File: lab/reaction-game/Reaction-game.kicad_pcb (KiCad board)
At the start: 2 copper layers, 92 x 72 mm, 10 parts, among them U1 atmega328p

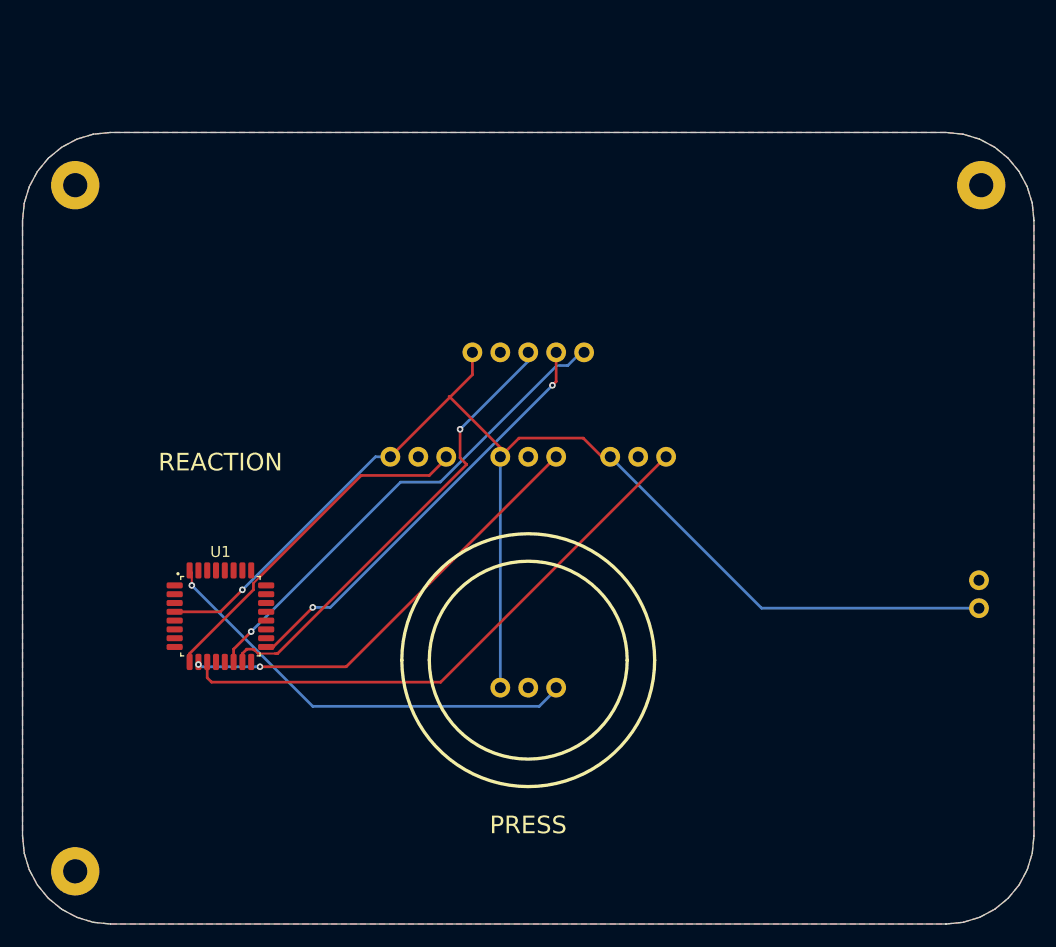
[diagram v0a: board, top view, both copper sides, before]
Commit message: lab: every board is a real board: an Arduino Nano and registry parts, routed, ready to order
The lab boards ran on simulation-only envelopes (labMcu, labDisplay, a battery). Now each is
an Arduino Nano on two sockets on the back (flashed over its USB, the image the app builds),
its lights LEDs through 1 kΩ, its knobs PTV09A pots, its display the MAX7219 eight-digit
module, its sensors an SHT31 and an SCD40 with their datasheets' support circuits, the FTDI
header for the serial console; the servo boards take 5 V on a screw terminal with a bulk
capacitor. All ten check complete with no errors or warnings, their firmware unchanged
(serial-device now on the 328P), and run in the lab without a fault (3 s each, dev host).

The registry: every interactive board must be ready to order and flash (publish.mjs refuses
one that is not; status simulation-only removed).

Claude-Session: https://claude.ai/code/session_01ATmMmxyrWxFwR3nTdXUrcx
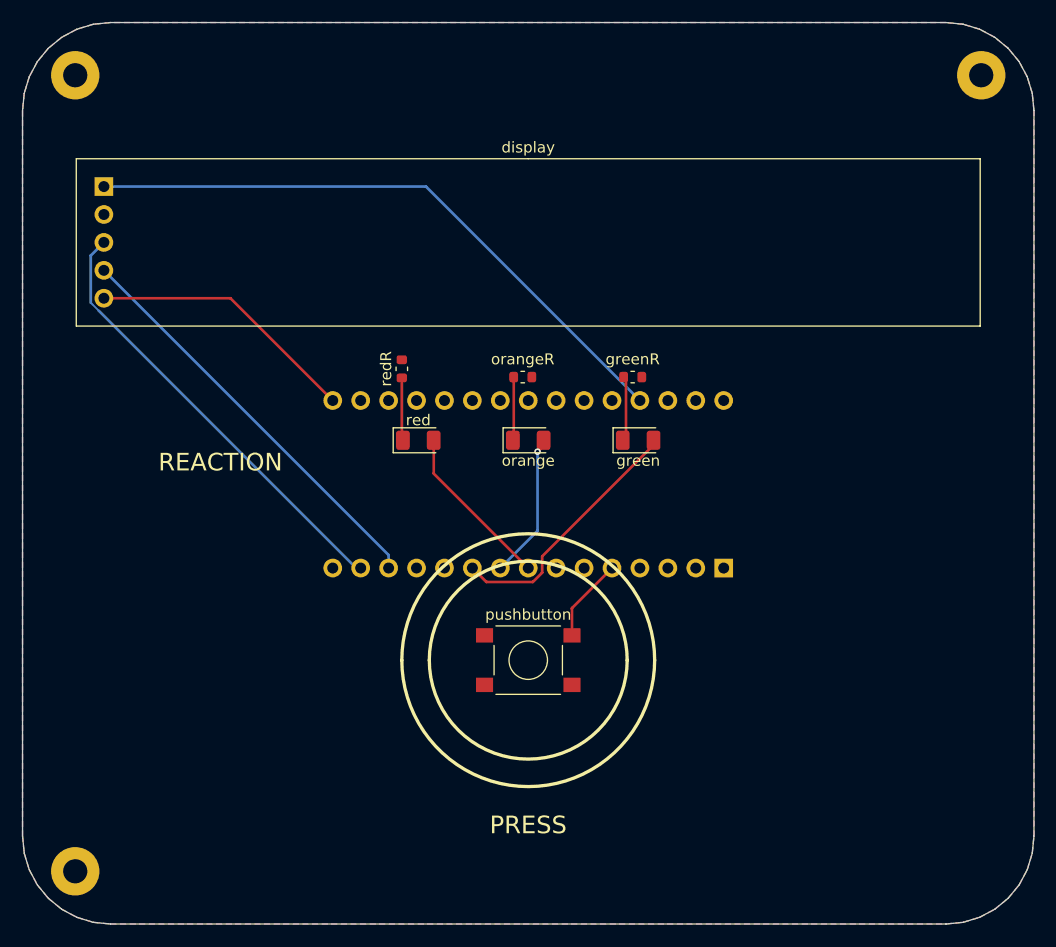
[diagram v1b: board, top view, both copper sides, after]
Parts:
- removed battery: battery, Regulated battery module
- removed button: button, Button module
- removed the display at (146.0, 142.0)
- removed the green at (156.0, 156.0)
- removed the orange at (146.0, 156.0)
- removed the red at (136.0, 156.0)
- added display: MAX7219 8-digit 7-segment LED display module, MAX7219_8digit_Module_Socket_1x05_P2.54mm, F.Cu at (146.0, 138.0)
- added green: green, LED_1206_3216Metric, F.Cu at (156.0, 156.0)
- added greenR: 1kohm, R_0603_1608Metric, F.Cu at (155.5, 150.2)
- added orange: orange, LED_1206_3216Metric, F.Cu at (146.0, 156.0)
- added orangeR: 1kohm, R_0603_1608Metric, F.Cu at (145.5, 150.2)
- added pushbutton: PTS645SM43SMTR92 LFS, SW_Tactile_SPST_6x6mm_SMD, F.Cu at (146.0, 176.0)
- added red: red, LED_1206_3216Metric, F.Cu at (136.0, 156.0)
- added redR: 1kohm, R_0603_1608Metric, F.Cu at (134.5, 149.5)
- U1: value atmega328p -> A000005; footprint TQFP-32_7x7mm_P0.8mm -> Arduino_Nano_Socket_2x15_P2.54mm_W15.24mm; moved to B.Cu
- moved U1 30.5 mm to (146.0, 160.0), turned to 90 degrees
- moved H2 10.0 mm to (104.8, 122.8)
- moved H3 10.0 mm to (187.2, 122.8)
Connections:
- U1 pad 10: ORANGE -> GREEN
- U1 pad 11: GREEN -> (no net)
- U1 pad 13: (no net) -> LOAD
- U1 pad 14: LOAD -> MOSI
- U1 pad 15: MOSI -> (no net)
- U1 pad 16: (no net) -> SCK
- U1 pad 17: SCK -> (no net)
- U1 pad 27: (no net) -> V5
- U1 pad 29: (no net) -> GND
- U1 pad 3: GND -> (no net)
- U1 pad 4: V5 -> GND
- U1 pad 5: (no net) -> PRESS
- U1 pad 8: (no net) -> RED
- U1 pad 9: RED -> ORANGE
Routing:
- net V5: track 117.1 -> 56.8 mm, vias 1 -> 0
- net PRESS: track 39.9 -> 7.64 mm, vias 1 -> 0
- net GREEN: track 51.8 -> 23.5 mm
- net ORANGE: track 40.5 -> 13.3 mm, vias 2 -> 1
- net RED: track 32.0 -> 15.2 mm
- net SCK: track 39.0 -> 24.7 mm, vias 2 -> 0
- net LOAD: track 44.2 -> 37.8 mm, vias 1 -> 0
- net GREEN_K: track 0.00 -> 5.96 mm
- net ORANGE_K: track 0.00 -> 5.78 mm
- net RED_K: track 0.00 -> 5.72 mm
- net MOSI: track 41.6 -> 40.5 mm, vias 1 -> 0
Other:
- board size 92 x 72 mm -> 92 x 82 mm

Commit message: registry: every board rebuilt with pcbkit main 4684674e6 - the bought part named on the board
pcbkit dc07fdfd6 writes the bought row's MPN and Manufacturer (the design's own kept as DesignMPN /
DesignManufacturer) and the build chooses parts before it places (6361ec104). Each of the 44 boards
was rebuilt (; the two P4 boards  only: their builds reroute pairs):
copper unchanged on all 44 (segments, arcs and vias counted before and after), placement kept; the
Arduino and lab boards now carry the parts the catalogue gives them. The check gains only the new
judgements: part-maker (a part bought from another maker) and part-missing on hand-fitted modules
(DS1 sockets); p4-touch-7 loses part-stale. The P4 boards keep their hole-clearance errors (a
reroute is Team 3's).

Claude-Session: https://claude.ai/code/session_01BAgp959tApA8aEg85EYgfb
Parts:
- H1, H2, H3: value (none) -> MountingHole_2.2mm_M2_Pad
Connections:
- pushbutton pad 2: PRESS -> GND
